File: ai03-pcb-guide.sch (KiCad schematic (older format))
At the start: 24 parts, among them SW1 SW_Push, U1 ATmega32U4-AU, Y1 16MHz

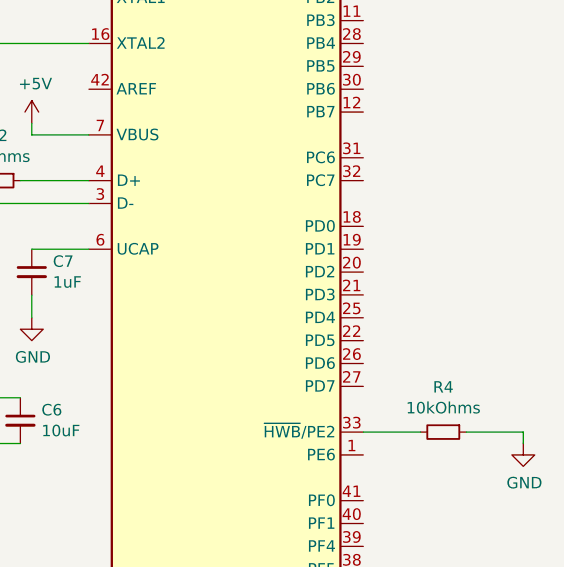
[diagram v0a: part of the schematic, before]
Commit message: added missing traces
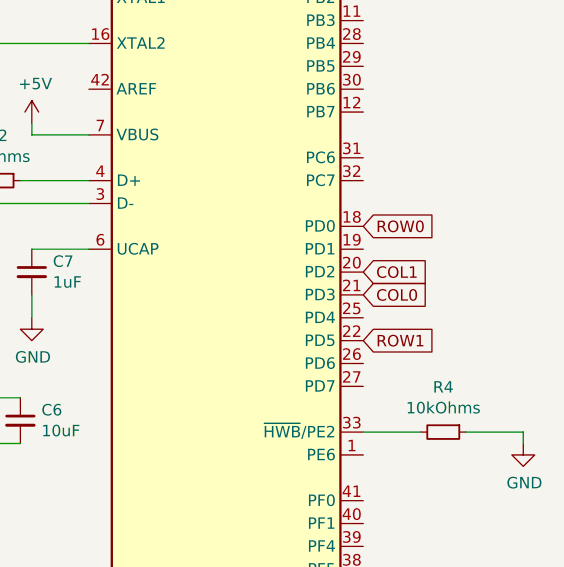
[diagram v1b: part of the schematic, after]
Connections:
- net COL0: now also U1.21 (PD3)
- net COL1: now also U1.20 (PD2)
- net ROW0: now also U1.18 (PD0)
- net ROW1: now also U1.22 (PD5)
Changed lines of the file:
@@
 Text GLabel 3350 2850 1    50   Input ~ 0
 COL1
+Text GLabel 9400 3350 2    50   Input ~ 0
+ROW1
+Text GLabel 9400 3150 2    50   Input ~ 0
+COL0
+Text GLabel 9400 3050 2    50   Input ~ 0
+COL1
+Text GLabel 9400 2850 2    50   Input ~ 0
+ROW0
 $EndSCHEMATC
